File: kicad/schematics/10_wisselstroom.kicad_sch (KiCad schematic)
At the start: 8 parts

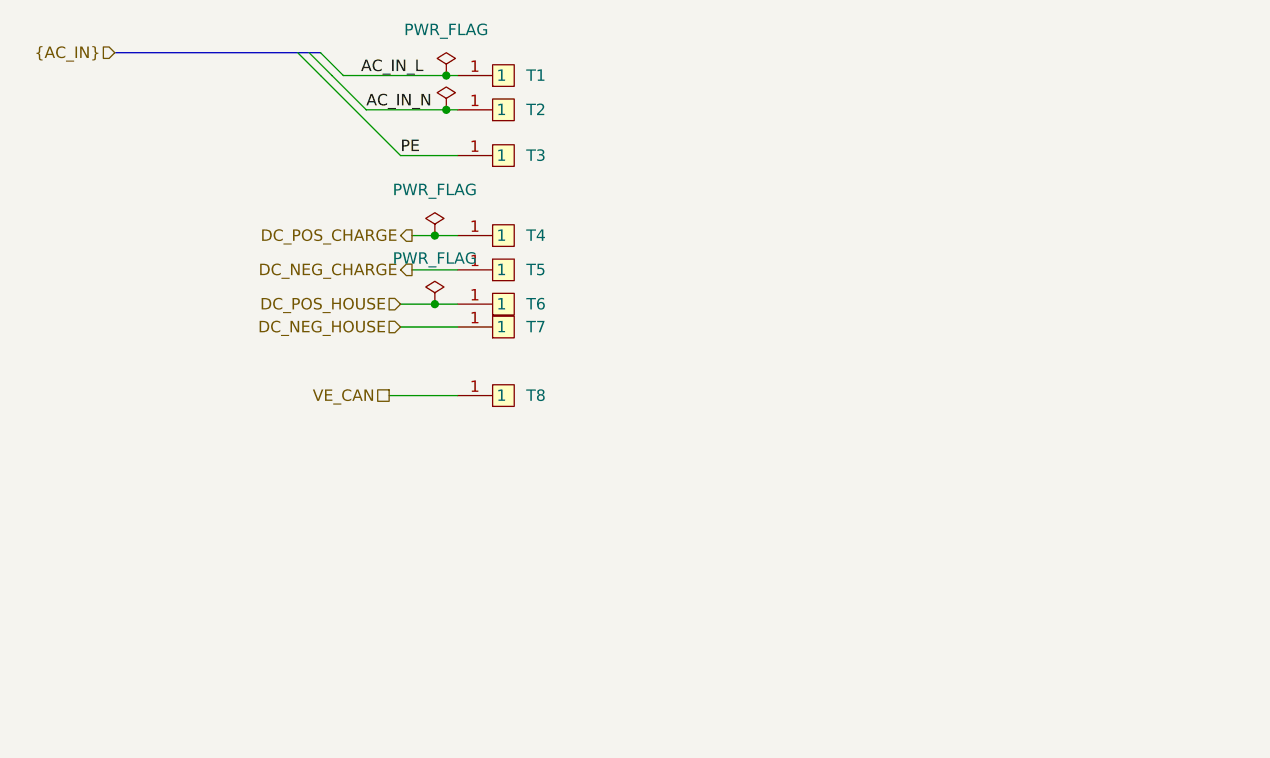
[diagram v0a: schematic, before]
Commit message: Introductie schema 15_energieconversie
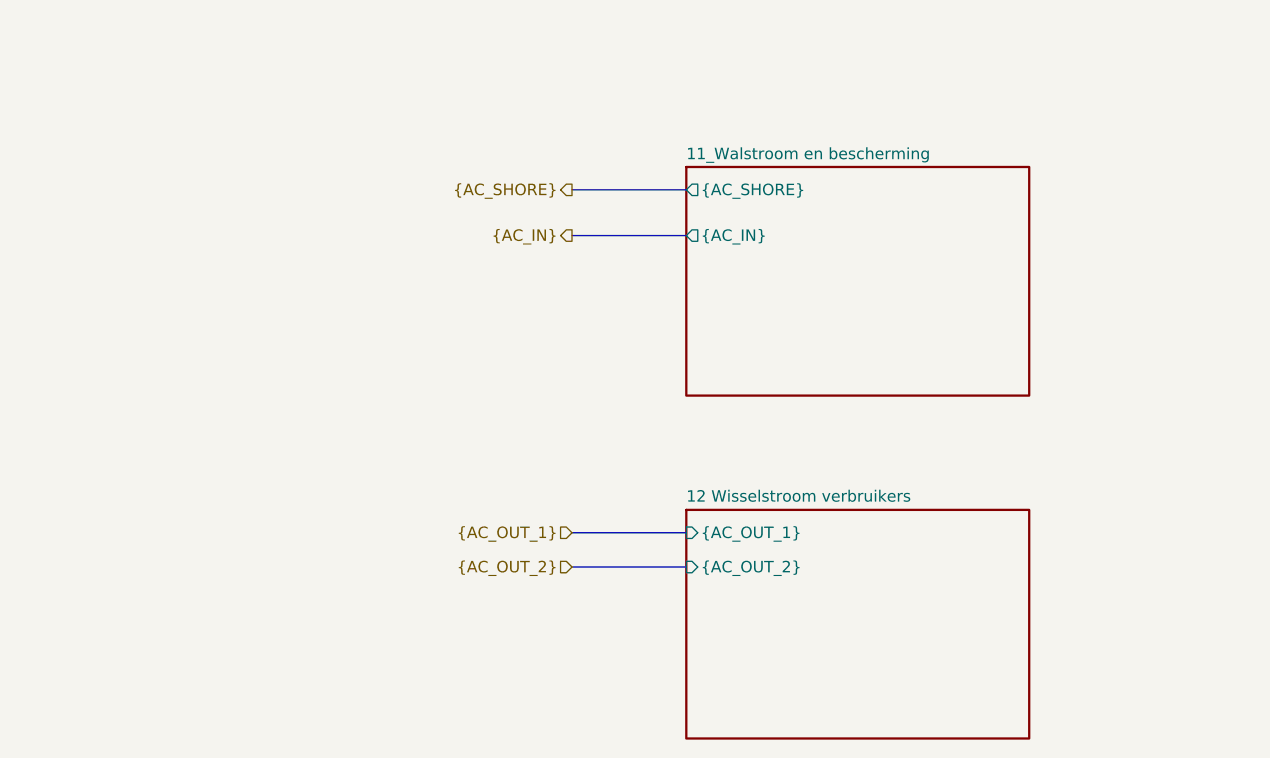
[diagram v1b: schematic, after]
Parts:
- removed T1, T2, T4, T5, T6, T7: (no value), symbol falkor-electrical:IF_Power_Input
- removed T3, T8: (no value), symbol falkor-electrical:IF_Passief
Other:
- added sheet 11_Walstroom en bescherming (11_walstroom_en_bescherming.kicad_sch)
- added sheet 12 Wisselstroom verbruikers (12_ac_verbruikers.kicad_sch)

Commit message: Schema's
00 toplevel stabiel
10 wisselstroom met subbladen stabiel
15 energieconversie stabiel
31 motor kern stabiel
32 motor sensoren stabiel
50 sensoren stabiel
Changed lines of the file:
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@@
 	(bus
 		(pts
-			(xy 76.2 78.74) (xy 88.9 78.74)
+			(xy 76.2 66.04) (xy 88.9 66.04)
 		)
 		(stroke
@@
 	(bus
 		(pts
-			(xy 76.2 45.72) (xy 88.9 45.72)
+			(xy 127 40.64) (xy 140.97 40.64)
 		)
 		(stroke
@@
 	(bus
 		(pts
-			(xy 76.2 82.55) (xy 88.9 82.55)
+			(xy 76.2 69.85) (xy 88.9 69.85)
 		)
 		(stroke
@@
 	)
 	(hierarchical_label "{AC_SHORE}"
-		(shape output)
+		(shape input)
 		(at 76.2 40.64 180)
 		(effects
@@
 	(hierarchical_label "{AC_OUT_1}"
 		(shape input)
-		(at 76.2 78.74 180)
+		(at 76.2 66.04 180)
 		(effects
 			(font
@@
 	(hierarchical_label "{AC_IN}"
 		(shape output)
-		(at 76.2 45.72 180)
+		(at 140.97 40.64 0)
 		(effects
 			(font
 				(size 1.27 1.27)
 			)
-			(justify right)
+			(justify left)
 		)
 	)
 	(hierarchical_label "{AC_OUT_2}"
 		(shape input)
-		(at 76.2 82.55 180)
+		(at 76.2 69.85 180)
 		(effects
 			(font
@@
 	(sheet
 		(at 88.9 38.1)
-		(size 38.1 25.4)
+		(size 38.1 12.7)
 		(exclude_from_sim no)
 		(in_bom yes)
@@
 		)
 		(property "Sheetname" "11_Walstroom en bescherming"
-			(at 88.9 37.3884 0)
+			(at 88.9 37.3376 0)
 			(show_name no)
 			(do_not_autoplace no)
@@
 		)
 		(property "Sheetfile" "11_walstroom_en_bescherming.kicad_sch"
-			(at 88.9 64.0846 0)
+			(at 88.9 51.4354 0)
 			(hide yes)
 			(show_name no)
@@
 			)
 		)
-		(pin "{AC_SHORE}" output
+		(pin "{AC_SHORE}" input
 			(at 88.9 40.64 180)
 			(effects
@@
 		)
 		(pin "{AC_IN}" output
-			(at 88.9 45.72 180)
+			(at 127 40.64 0)
 			(effects
 				(font
 					(size 1.27 1.27)
 				)
-				(justify left)
+				(justify right)
 			)
 		)
@@
 	)
 	(sheet
-		(at 88.9 76.2)
-		(size 38.1 25.4)
+		(at 88.9 63.5)
+		(size 38.1 12.7)
 		(exclude_from_sim no)
 		(in_bom yes)
@@
 		)
 		(property "Sheetname" "12 Wisselstroom verbruikers"
-			(at 88.9 75.4376 0)
+			(at 88.9 62.7376 0)
 			(show_name no)
 			(do_not_autoplace no)
@@
 		)
 		(property "Sheetfile" "12_ac_verbruikers.kicad_sch"
-			(at 88.9 102.2354 0)
+			(at 88.9 76.8354 0)
 			(hide yes)
 			(show_name no)
@@
 		)
 		(pin "{AC_OUT_1}" input
-			(at 88.9 78.74 180)
+			(at 88.9 66.04 180)
 			(effects
 				(font
@@
 		)
 		(pin "{AC_OUT_2}" input
-			(at 88.9 82.55 180)
+			(at 88.9 69.85 180)
 			(effects
 				(font
